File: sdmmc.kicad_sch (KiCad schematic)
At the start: 18 parts, among them J4 Micro_SD_Card_Det2

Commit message: did stuff
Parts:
- renumbered C50 to C113, C49 to C114, D8 to D40, D9 to D41, D10 to D42, D11 to D43, D12 to D44, D13 to D45, D14 to D46, R52 to R84, R51 to R85, R50 to R86, R49 to R87, R48 to R88, R47 to R89, R46 to R90, R45 to R91
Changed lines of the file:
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@@
 		(dnp no)
 		(fields_autoplaced yes)
-		(property "Reference" "R52"
+		(property "Reference" "R84"
 			(at 116.84 68.5799 0)
 			(effects
@@
 			(project "netdaq"
 				(path "/2970f661-65ab-4e2b-aeda-d76d1044f2b8/1813fba9-8b3b-4d19-ab19-e743aa636a8b"
-					(reference "R52")
+					(reference "R84")
 					(unit 1)
 				)
@@
 		(dnp no)
 		(fields_autoplaced yes)
-		(property "Reference" "D8"
+		(property "Reference" "D40"
 			(at 120.65 107.9499 90)
 			(effects
@@
 			(project ""
 				(path "/2970f661-65ab-4e2b-aeda-d76d1044f2b8/1813fba9-8b3b-4d19-ab19-e743aa636a8b"
-					(reference "D8")
+					(reference "D40")
 					(unit 1)
 				)
@@
 		(dnp no)
 		(fields_autoplaced yes)
-		(property "Reference" "#PWR090"
+		(property "Reference" "#PWR0198"
 			(at 204.47 120.65 0)
 			(effects
@@
 			(project ""
 				(path "/2970f661-65ab-4e2b-aeda-d76d1044f2b8/1813fba9-8b3b-4d19-ab19-e743aa636a8b"
-					(reference "#PWR090")
+					(reference "#PWR0198")
 					(unit 1)
 				)
@@
 		(dnp no)
 		(fields_autoplaced yes)
-		(property "Reference" "D14"
+		(property "Reference" "D46"
 			(at 173.99 107.9499 90)
 			(effects
@@
 			(project "netdaq"
 				(path "/2970f661-65ab-4e2b-aeda-d76d1044f2b8/1813fba9-8b3b-4d19-ab19-e743aa636a8b"
-					(reference "D14")
+					(reference "D46")
 					(unit 1)
 				)
@@
 		(dnp no)
 		(fields_autoplaced yes)
-		(property "Reference" "#PWR098"
+		(property "Reference" "#PWR0193"
 			(at 135.89 120.65 0)
 			(effects
@@
 			(project "netdaq"
 				(path "/2970f661-65ab-4e2b-aeda-d76d1044f2b8/1813fba9-8b3b-4d19-ab19-e743aa636a8b"
-					(reference "#PWR098")
+					(reference "#PWR0193")
 					(unit 1)
 				)
@@
 		(dnp no)
 		(fields_autoplaced yes)
-		(property "Reference" "R51"
+		(property "Reference" "R85"
 			(at 125.73 68.5799 0)
 			(effects
@@
 			(project "netdaq"
 				(path "/2970f661-65ab-4e2b-aeda-d76d1044f2b8/1813fba9-8b3b-4d19-ab19-e743aa636a8b"
-					(reference "R51")
+					(reference "R85")
 					(unit 1)
 				)
@@
 		(dnp no)
 		(fields_autoplaced yes)
-		(property "Reference" "R50"
+		(property "Reference" "R86"
 			(at 134.62 68.5799 0)
 			(effects
@@
 			(project "netdaq"
 				(path "/2970f661-65ab-4e2b-aeda-d76d1044f2b8/1813fba9-8b3b-4d19-ab19-e743aa636a8b"
-					(reference "R50")
+					(reference "R86")
 					(unit 1)
 				)
@@
 		(dnp no)
 		(fields_autoplaced yes)
-		(property "Reference" "#PWR097"
+		(property "Reference" "#PWR0192"
 			(at 127 120.65 0)
 			(effects
@@
 			(project "netdaq"
 				(path "/2970f661-65ab-4e2b-aeda-d76d1044f2b8/1813fba9-8b3b-4d19-ab19-e743aa636a8b"
-					(reference "#PWR097")
+					(reference "#PWR0192")
 					(unit 1)
 				)
@@
 		(dnp no)
 		(fields_autoplaced yes)
-		(property "Reference" "#PWR099"
+		(property "Reference" "#PWR0194"
 			(at 144.78 120.65 0)
 			(effects
@@
 			(project "netdaq"
 				(path "/2970f661-65ab-4e2b-aeda-d76d1044f2b8/1813fba9-8b3b-4d19-ab19-e743aa636a8b"
-					(reference "#PWR099")
+					(reference "#PWR0194")
 					(unit 1)
 				)
@@
 		(dnp no)
 		(fields_autoplaced yes)
-		(property "Reference" "#PWR095"
+		(property "Reference" "#PWR0188"
 			(at 137.16 64.77 0)
 			(effects
@@
 			(project "netdaq"
 				(path "/2970f661-65ab-4e2b-aeda-d76d1044f2b8/1813fba9-8b3b-4d19-ab19-e743aa636a8b"
-					(reference "#PWR095")
+					(reference "#PWR0188")
 					(unit 1)
 				)
@@
 		(dnp no)
 		(fields_autoplaced yes)
-		(property "Reference" "#PWR092"
+		(property "Reference" "#PWR0190"
 			(at 195.58 76.2 0)
 			(effects
@@
 			(project "netdaq"
 				(path "/2970f661-65ab-4e2b-aeda-d76d1044f2b8/1813fba9-8b3b-4d19-ab19-e743aa636a8b"
-					(reference "#PWR092")
+					(reference "#PWR0190")
 					(unit 1)
 				)
@@
 		(dnp no)
 		(fields_autoplaced yes)
-		(property "Reference" "#PWR091"
+		(property "Reference" "#PWR0199"
 			(at 252.73 120.65 0)
 			(effects
@@
 			(project "netdaq"
 				(path "/2970f661-65ab-4e2b-aeda-d76d1044f2b8/1813fba9-8b3b-4d19-ab19-e743aa636a8b"
-					(reference "#PWR091")
+					(reference "#PWR0199")
 					(unit 1)
 				)
@@
 		(dnp no)
 		(fields_autoplaced yes)
-		(property "Reference" "#PWR093"
+		(property "Reference" "#PWR0189"
 			(at 184.15 76.2 0)
 			(effects
@@
 			(project "netdaq"
 				(path "/2970f661-65ab-4e2b-aeda-d76d1044f2b8/1813fba9-8b3b-4d19-ab19-e743aa636a8b"
-					(reference "#PWR093")
+					(reference "#PWR0189")
 					(unit 1)
 				)
@@
 		(dnp no)
 		(fields_autoplaced yes)
-		(property "Reference" "#PWR096"
+		(property "Reference" "#PWR0191"
 			(at 118.11 120.65 0)
 			(effects
@@
 			(project "netdaq"
 				(path "/2970f661-65ab-4e2b-aeda-d76d1044f2b8/1813fba9-8b3b-4d19-ab19-e743aa636a8b"
-					(reference "#PWR096")
+					(reference "#PWR0191")
 					(unit 1)
 				)
@@
 		(dnp no)
 		(fields_autoplaced yes)
-		(property "Reference" "#PWR0100"
+		(property "Reference" "#PWR0195"
 			(at 153.67 120.65 0)
 			(effects
@@
 			(project "netdaq"
 				(path "/2970f661-65ab-4e2b-aeda-d76d1044f2b8/1813fba9-8b3b-4d19-ab19-e743aa636a8b"
-					(reference "#PWR0100")
+					(reference "#PWR0195")
 					(unit 1)
 				)
@@
 		(dnp no)
 		(fields_autoplaced yes)
-		(property "Reference" "D12"
+		(property "Reference" "D44"
 			(at 156.21 107.9499 90)
 			(effects
@@
 			(project "netdaq"
 				(path "/2970f661-65ab-4e2b-aeda-d76d1044f2b8/1813fba9-8b3b-4d19-ab19-e743aa636a8b"
-					(reference "D12")
+					(reference "D44")
 					(unit 1)
 				)
@@
 		(dnp no)
 		(fields_autoplaced yes)
-		(property "Reference" "R49"
+		(property "Reference" "R87"
 			(at 143.51 68.5799 0)
 			(effects
@@
 			(project "netdaq"
 				(path "/2970f661-65ab-4e2b-aeda-d76d1044f2b8/1813fba9-8b3b-4d19-ab19-e743aa636a8b"
-					(reference "R49")
+					(reference "R87")
 					(unit 1)
 				)
@@
 		(dnp no)
 		(fields_autoplaced yes)
-		(property "Reference" "R46"
+		(property "Reference" "R90"
 			(at 170.18 68.5799 0)
 			(effects
@@
 			(project ""
 				(path "/2970f661-65ab-4e2b-aeda-d76d1044f2b8/1813fba9-8b3b-4d19-ab19-e743aa636a8b"
-					(reference "R46")
+					(reference "R90")
 					(unit 1)
 				)
@@
 		(dnp no)
 		(fields_autoplaced yes)
-		(property "Reference" "R47"
+		(property "Reference" "R89"
 			(at 161.29 68.5799 0)
 			(effects
@@
 			(project "netdaq"
 				(path "/2970f661-65ab-4e2b-aeda-d76d1044f2b8/1813fba9-8b3b-4d19-ab19-e743aa636a8b"
-					(reference "R47")
+					(reference "R89")
 					(unit 1)
 				)
@@
 		(dnp no)
 		(fields_autoplaced yes)
-		(property "Reference" "D11"
+		(property "Reference" "D43"
 			(at 147.32 107.9499 90)
 			(effects
@@
 			(project "netdaq"
 				(path "/2970f661-65ab-4e2b-aeda-d76d1044f2b8/1813fba9-8b3b-4d19-ab19-e743aa636a8b"
-					(reference "D11")
+					(reference "D43")
 					(unit 1)
 				)
@@
 		(dnp no)
 		(fields_autoplaced yes)
-		(property "Reference" "#PWR0105"
+		(property "Reference" "#PWR0197"
 			(at 171.45 120.65 0)
 			(effects
@@
 			(project "netdaq"
 				(path "/2970f661-65ab-4e2b-aeda-d76d1044f2b8/1813fba9-8b3b-4d19-ab19-e743aa636a8b"
-					(reference "#PWR0105")
+					(reference "#PWR0197")
 					(unit 1)
 				)
@@
 		(dnp no)
 		(fields_autoplaced yes)
-		(property "Reference" "#PWR094"
+		(property "Reference" "#PWR0187"
 			(at 180.34 60.96 0)
 			(effects
@@
 			(project ""
 				(path "/2970f661-65ab-4e2b-aeda-d76d1044f2b8/1813fba9-8b3b-4d19-ab19-e743aa636a8b"
-					(reference "#PWR094")
+					(reference "#PWR0187")
 					(unit 1)
 				)
@@
 		(dnp no)
 		(fields_autoplaced yes)
-		(property "Reference" "D9"
+		(property "Reference" "D41"
 			(at 129.54 107.9499 90)
 			(effects
@@
 			(project "netdaq"
 				(path "/2970f661-65ab-4e2b-aeda-d76d1044f2b8/1813fba9-8b3b-4d19-ab19-e743aa636a8b"
-					(reference "D9")
+					(reference "D41")
 					(unit 1)
 				)
@@
 		(dnp no)
 		(fields_autoplaced yes)
-		(property "Reference" "C50"
+		(property "Reference" "C113"
 			(at 187.96 63.4999 0)
 			(effects
@@
 			(project "netdaq"
 				(path "/2970f661-65ab-4e2b-aeda-d76d1044f2b8/1813fba9-8b3b-4d19-ab19-e743aa636a8b"
-					(reference "C50")
+					(reference "C113")
 					(unit 1)
 				)
@@
 		(dnp no)
 		(fields_autoplaced yes)
-		(property "Reference" "D13"
+		(property "Reference" "D45"
 			(at 165.1 107.9499 90)
 			(effects
@@
 			(project "netdaq"
 				(path "/2970f661-65ab-4e2b-aeda-d76d1044f2b8/1813fba9-8b3b-4d19-ab19-e743aa636a8b"
-					(reference "D13")
+					(reference "D45")
 					(unit 1)
 				)
@@
 		(dnp no)
 		(fields_autoplaced yes)
-		(property "Reference" "R45"
+		(property "Reference" "R91"
 			(at 255.27 107.9499 0)
 			(effects
@@
 			(project ""
 				(path "/2970f661-65ab-4e2b-aeda-d76d1044f2b8/1813fba9-8b3b-4d19-ab19-e743aa636a8b"
-					(reference "R45")
+					(reference "R91")
 					(unit 1)
 				)
@@
 		(dnp no)
 		(fields_autoplaced yes)
-		(property "Reference" "R48"
+		(property "Reference" "R88"
 			(at 152.4 68.5799 0)
 			(effects
@@
 			(project "netdaq"
 				(path "/2970f661-65ab-4e2b-aeda-d76d1044f2b8/1813fba9-8b3b-4d19-ab19-e743aa636a8b"
-					(reference "R48")
+					(reference "R88")
 					(unit 1)
 				)
@@
 		(dnp no)
 		(fields_autoplaced yes)
-		(property "Reference" "C49"
+		(property "Reference" "C114"
 			(at 199.39 63.4999 0)
 			(effects
@@
 			(project ""
 				(path "/2970f661-65ab-4e2b-aeda-d76d1044f2b8/1813fba9-8b3b-4d19-ab19-e743aa636a8b"
-					(reference "C49")
+					(reference "C114")
 					(unit 1)
 				)
@@
 		(dnp no)
 		(fields_autoplaced yes)
-		(property "Reference" "#PWR0104"
+		(property "Reference" "#PWR0196"
 			(at 162.56 120.65 0)
 			(effects
@@
 			(project "netdaq"
 				(path "/2970f661-65ab-4e2b-aeda-d76d1044f2b8/1813fba9-8b3b-4d19-ab19-e743aa636a8b"
-					(reference "#PWR0104")
+					(reference "#PWR0196")
 					(unit 1)
 				)
@@
 		(dnp no)
 		(fields_autoplaced yes)
-		(property "Reference" "D10"
+		(property "Reference" "D42"
 			(at 138.43 107.9499 90)
 			(effects
@@
 			(project "netdaq"
 				(path "/2970f661-65ab-4e2b-aeda-d76d1044f2b8/1813fba9-8b3b-4d19-ab19-e743aa636a8b"
-					(reference "D10")
-					(unit 1)
-				)
+					(reference "D42")
+					(unit 1)
+				)

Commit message: many stuffs
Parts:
- removed J4: Micro_SD_Card_Det2, Connector_Card:microSD_HC_Hirose_DM3AT-SF-PEJM5, symbol Connector:Micro_SD_Card_Det2
- added U15: MLD-TF PUSH-H18, C52750848:SD-SMD_MLD-TF-PUSH-H18, symbol C52750848:MLD-TFPUSH-H18
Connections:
- net +3.3V: now also U15.4 (VDD)
- net GND: now also U15.6 (VSS)
- net MMC.SDCD: now also U15.CD
- net MMC.SDCK: now also U15.5 (CLX)
- net MMC.SDCMD: now also U15.3 (CMD)
- net MMC.SDDAT0: now also U15.7 (DAT0)
- net MMC.SDDAT1: now also U15.8 (DAT1)
- net MMC.SDDAT2: now also U15.1 (DAT2)
- net MMC.SDDAT3: now also U15.2 (CD/DAT3)
- net at R91.1: now also U15.10 (EH), U15.11 (EH), U15.12 (EH), U15.13 (EH)
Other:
- moved on the sheet: R91
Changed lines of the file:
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@@
 	)
 	(junction
-		(at 204.47 104.14)
+		(at 153.67 86.36)
 		(diameter 0)
 		(color 0 0 0 0)
 	)
 	(junction
-		(at 153.67 86.36)
+		(at 236.22 99.06)
 		(diameter 0)
 		(color 0 0 0 0)
@@
 	)
 	(junction
+		(at 236.22 101.6)
+		(diameter 0)
+		(color 0 0 0 0)
+	)
+	(junction
 		(at 149.86 86.36)
 		(diameter 0)
@@
 	)
 	(junction
+		(at 236.22 83.82)
+		(diameter 0)
+		(color 0 0 0 0)
+	)
+	(junction
 		(at 118.11 101.6)
 		(diameter 0)
@@
 	(wire
 		(pts
-			(xy 204.47 93.98) (xy 204.47 104.14)
+			(xy 204.47 93.98) (xy 204.47 114.3)
 		)
 		(stroke
@@
 	(wire
 		(pts
+			(xy 236.22 101.6) (xy 236.22 105.41)
+		)
+		(stroke
+			(width 0)
+			(type default)
+		)
+	)
+	(wire
+		(pts
 			(xy 180.34 59.69) (xy 184.15 59.69)
 		)
@@
 	(wire
 		(pts
+			(xy 236.22 99.06) (xy 234.95 99.06)
+		)
+		(stroke
+			(width 0)
+			(type default)
+		)
+	)
+	(wire
+		(pts
 			(xy 153.67 86.36) (xy 207.01 86.36)
 		)
@@
 	(wire
 		(pts
-			(xy 252.73 105.41) (xy 252.73 104.14)
+			(xy 140.97 64.77) (xy 149.86 64.77)
 		)
 		(stroke
@@
 	(wire
 		(pts
-			(xy 140.97 64.77) (xy 149.86 64.77)
+			(xy 236.22 81.28) (xy 236.22 83.82)
 		)
 		(stroke
@@
 	(wire
 		(pts
-			(xy 252.73 113.03) (xy 252.73 114.3)
+			(xy 236.22 113.03) (xy 236.22 114.3)
+		)
+		(stroke
+			(width 0)
+			(type default)
+		)
+	)
+	(wire
+		(pts
+			(xy 234.95 81.28) (xy 236.22 81.28)
 		)
 		(stroke
@@
 	(wire
 		(pts
-			(xy 204.47 104.14) (xy 207.01 104.14)
-		)
-		(stroke
-			(width 0)
-			(type default)
-		)
-	)
-	(wire
-		(pts
 			(xy 100.33 96.52) (xy 132.08 96.52)
 		)
@@
 	(wire
 		(pts
+			(xy 234.95 83.82) (xy 236.22 83.82)
+		)
+		(stroke
+			(width 0)
+			(type default)
+		)
+	)
+	(wire
+		(pts
 			(xy 114.3 73.66) (xy 114.3 101.6)
 		)
@@
 	(wire
 		(pts
-			(xy 250.19 104.14) (xy 252.73 104.14)
+			(xy 234.95 101.6) (xy 236.22 101.6)
 		)
 		(stroke
@@
 	(wire
 		(pts
-			(xy 135.89 96.52) (xy 207.01 96.52)
+			(xy 236.22 101.6) (xy 236.22 99.06)
 		)
 		(stroke
@@
 	(wire
 		(pts
-			(xy 162.56 83.82) (xy 207.01 83.82)
+			(xy 236.22 83.82) (xy 236.22 99.06)
 		)
 		(stroke
@@
 	(wire
 		(pts
-			(xy 135.89 113.03) (xy 135.89 114.3)
+			(xy 135.89 96.52) (xy 207.01 96.52)
 		)
 		(stroke
@@
 	(wire
 		(pts
-			(xy 123.19 99.06) (xy 127 99.06)
+			(xy 162.56 83.82) (xy 207.01 83.82)
 		)
 		(stroke
@@
 	(wire
 		(pts
-			(xy 204.47 104.14) (xy 204.47 114.3)
+			(xy 135.89 113.03) (xy 135.89 114.3)
+		)
+		(stroke
+			(width 0)
+			(type default)
+		)
+	)
+	(wire
+		(pts
+			(xy 123.19 99.06) (xy 127 99.06)
 		)
 		(stroke
@@
 	)
 	(symbol
+		(lib_id "C52750848:MLD-TFPUSH-H18")
+		(at 219.71 93.98 0)
+		(unit 1)
+		(body_style 1)
+		(exclude_from_sim no)
+		(in_bom yes)
+		(on_board yes)
+		(in_pos_files yes)
+		(dnp no)
+		(fields_autoplaced yes)
+		(property "Reference" "U15"
+			(at 220.98 73.66 0)
+			(show_name no)
+			(do_not_autoplace no)
+			(effects
+				(font
+					(size 1.27 1.27)
+				)
+			)
+		)
+		(property "Value" "MLD-TF PUSH-H18"
+			(at 220.98 76.2 0)
+			(show_name no)
+			(do_not_autoplace no)
+			(effects
+				(font
+					(size 1.27 1.27)
+				)
+			)
+		)
+		(property "Footprint" "C52750848:SD-SMD_MLD-TF-PUSH-H18"
+			(at 219.71 109.22 0)
+			(hide yes)
+			(show_name no)
+			(do_not_autoplace no)
+			(effects
+				(font
+					(size 1.27 1.27)
+				)
+			)
+		)
+		(property "Datasheet" ""
+			(at 219.71 93.98 0)
+			(hide yes)
+			(show_name no)
+			(do_not_autoplace no)
+			(effects
+				(font
+					(size 1.27 1.27)
+				)
+			)
+		)
+		(property "Description" ""
+			(at 219.71 93.98 0)
+			(hide yes)
+			(show_name no)
+			(do_not_autoplace no)
+			(effects
+				(font
+					(size 1.27 1.27)
+				)
+			)
+		)
+		(property "LCSC Part" "C52750848"
+			(at 219.71 111.76 0)
+			(hide yes)
+			(show_name no)
+			(do_not_autoplace no)
+			(effects
+				(font
+					(size 1.27 1.27)
+				)
+			)
+		)
+		(pin "CD"
+		)
+		(pin "11"
+		)
+		(pin "13"
+		)
+		(pin "10"
+		)
+		(pin "12"
+		)
+		(pin "8"
+		)
+		(pin "7"
+		)
+		(pin "6"
+		)
+		(pin "5"
+		)
+		(pin "2"
+		)
+		(pin "4"
+		)
+		(pin "1"
+		)
+		(pin "3"
+		)
+		(instances
+			(project "netdaq"
+				(path "/2970f661-65ab-4e2b-aeda-d76d1044f2b8/1813fba9-8b3b-4d19-ab19-e743aa636a8b"
+					(reference "U15")
+					(unit 1)
+				)
+			)
+		)
+	)
+	(symbol
 		(lib_id "Device:R")
 		(at 132.08 69.85 0)
@@
 	(symbol
 		(lib_id "power:GND")
-		(at 252.73 114.3 0)
+		(at 236.22 114.3 0)
 		(unit 1)
 		(body_style 1)
@@
 		(fields_autoplaced yes)
 		(property "Reference" "#PWR0199"
-			(at 252.73 120.65 0)
+			(at 236.22 120.65 0)
 			(hide yes)
 			(show_name no)
@@
 		)
 		(property "Value" "GND"
-			(at 252.73 119.38 0)
+			(at 236.22 119.38 0)
 			(show_name no)
 			(do_not_autoplace no)
@@
 		)
 		(property "Footprint" ""
-			(at 252.73 114.3 0)
+			(at 236.22 114.3 0)
 			(hide yes)
 			(show_name no)
@@
 		)
 		(property "Datasheet" ""
-			(at 252.73 114.3 0)
+			(at 236.22 114.3 0)
 			(hide yes)
 			(show_name no)
@@
 		)
 		(property "Description" "Power symbol creates a global label with name \"GND\" , ground"
-			(at 252.73 114.3 0)
+			(at 236.22 114.3 0)
 			(hide yes)
 			(show_name no)
@@
 	)
 	(symbol
-		(lib_id "Connector:Micro_SD_Card_Det2")
-		(at 229.87 91.44 0)
-		(unit 1)
-		(body_style 1)
-		(exclude_from_sim no)
-		(in_bom yes)
-		(on_board yes)
-		(in_pos_files yes)
-		(dnp no)
-		(fields_autoplaced yes)
-		(property "Reference" "J4"
-			(at 230.505 69.85 0)
-			(show_name no)
-			(do_not_autoplace no)
-			(effects
-				(font
-					(size 1.27 1.27)
-				)
-			)
-		)
-		(property "Value" "Micro_SD_Card_Det2"
-			(at 230.505 72.39 0)
-			(show_name no)
-			(do_not_autoplace no)
-			(effects
-				(font
-					(size 1.27 1.27)
-				)
-			)
-		)
-		(property "Footprint" "Connector_Card:microSD_HC_Hirose_DM3AT-SF-PEJM5"
-			(at 281.94 73.66 0)
-			(hide yes)
-			(show_name no)
-			(do_not_autoplace no)
-			(effects
-				(font
-					(size 1.27 1.27)
-				)
-			)
-		)
-		(property "Datasheet" "https://www.hirose.com/en/product/document?clcode=&productname=&series=DM3&documenttype=Catalog&lang=en&documentid=D49662_en"
-			(at 232.41 88.9 0)
-			(hide yes)
-			(show_name no)
-			(do_not_autoplace no)
-			(effects
-				(font
-					(size 1.27 1.27)
-				)
-			)
-		)
-		(property "Description" "Micro SD Card Socket with two card detection pins"
-			(at 229.87 91.44 0)
-			(hide yes)
-			(show_name no)
-			(do_not_autoplace no)
-			(effects
-				(font
-					(size 1.27 1.27)
-				)
-			)
-		)
-		(pin "9"
-		)
-		(pin "8"
-		)
-		(pin "6"
-		)
-		(pin "7"
-		)
-		(pin "5"
-		)
-		(pin "4"
-		)
-		(pin "10"
-		)
-		(pin "3"
-		)
-		(pin "11"
-		)
-		(pin "1"
-		)
-		(pin "2"
-		)
-		(instances
-			(project "netdaq"
-				(path "/2970f661-65ab-4e2b-aeda-d76d1044f2b8/1813fba9-8b3b-4d19-ab19-e743aa636a8b"
-					(reference "J4")
-					(unit 1)
-				)
-			)
-		)
-	)
-	(symbol
 		(lib_id "power:GND")
 		(at 118.11 114.3 0)
@@
 	(symbol
 		(lib_id "Device:R")
-		(at 252.73 109.22 0)
+		(at 236.22 109.22 0)
 		(unit 1)
 		(body_style 1)
@@
 		(fields_autoplaced yes)
 		(property "Reference" "R91"
-			(at 255.27 107.9499 0)
+			(at 238.76 107.9499 0)
 			(show_name no)
 			(do_not_autoplace no)
@@
 		)
 		(property "Value" "100k"
-			(at 255.27 110.4899 0)
+			(at 238.76 110.4899 0)
 			(show_name no)
 			(do_not_autoplace no)
@@
 		)
 		(property "Footprint" "Resistor_SMD:R_0402_1005Metric"
-			(at 250.952 109.22 90)
+			(at 234.442 109.22 90)
 			(hide yes)
 			(show_name no)
@@
 		)
 		(property "Datasheet" ""
-			(at 252.73 109.22 0)
+			(at 236.22 109.22 0)
 			(hide yes)
 			(show_name no)
@@
 		)
 		(property "Description" "Resistor"
-			(at 252.73 109.22 0)
+			(at 236.22 109.22 0)
 			(hide yes)
 			(show_name no)

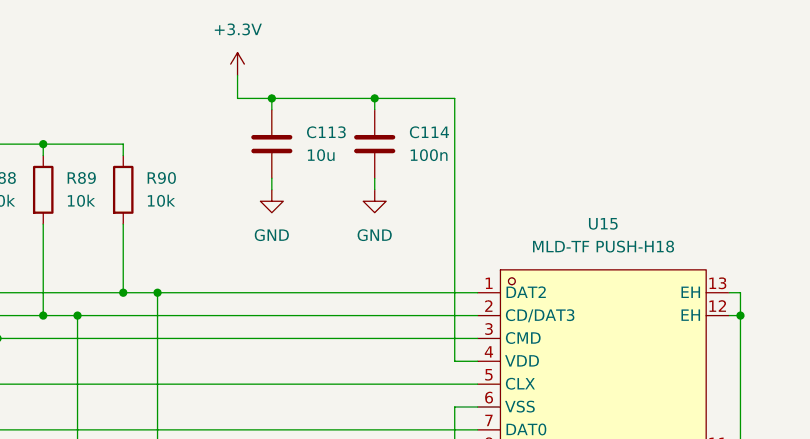
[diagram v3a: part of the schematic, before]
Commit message: did a bunch of bom matching to lcsc
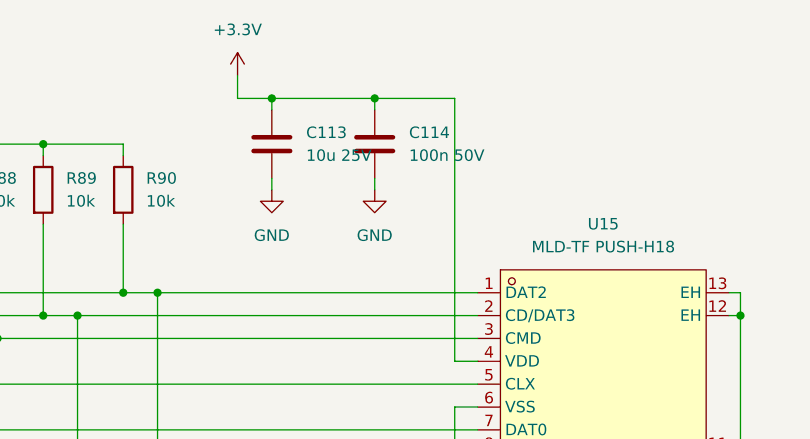
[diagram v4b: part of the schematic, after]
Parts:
- C113: value 10u -> 10u 25V; LCSC (none) -> C15850; LCSC Basic/Pref (none) -> x; LCSC Part (none) -> C15850
- C114: value 100n -> 100n 50V; LCSC (none) -> C307331; LCSC Basic/Pref (none) -> x; LCSC Part (none) -> C307331
- R84, R85, R86, R87, R88, R89, R90: LCSC (none) -> C25744; LCSC Basic/Pref (none) -> x; LCSC Part (none) -> C25744
- R91: LCSC (none) -> C25741; LCSC Basic/Pref (none) -> x; LCSC Part (none) -> C25741

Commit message: bunch of stuff
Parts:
- removed D40, D41, D42, D43, D44, D45, D46: D_TVS, symbol Device:D_TVS
- added U16, U17: TPUSBLC6-4SC6, Package_TO_SOT_SMD:SOT-23-6_Handsoldering, symbol Library:TPUSBLC6-4SC6
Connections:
- net +3.3V: now also U16.5, U17.5
- net GND: now also U16.2 (VSS), U17.2 (VSS)
- net MMC.SDCD: now also U16.1
- net MMC.SDCK: now also U16.3
- net MMC.SDCMD: now also U17.1
- net MMC.SDDAT0: now also U16.4
- net MMC.SDDAT1: now also U16.6
- net MMC.SDDAT2: now also U17.4
- net MMC.SDDAT3: now also U17.6
- no-connect marks 0 -> 1
